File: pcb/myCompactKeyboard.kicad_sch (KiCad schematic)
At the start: 245 parts, among them J1 OLED_128x64, SW1 RotaryEncoder_Switch, SW2 RotaryEncoder_Switch, U1 Raspberry_Pi_Pico

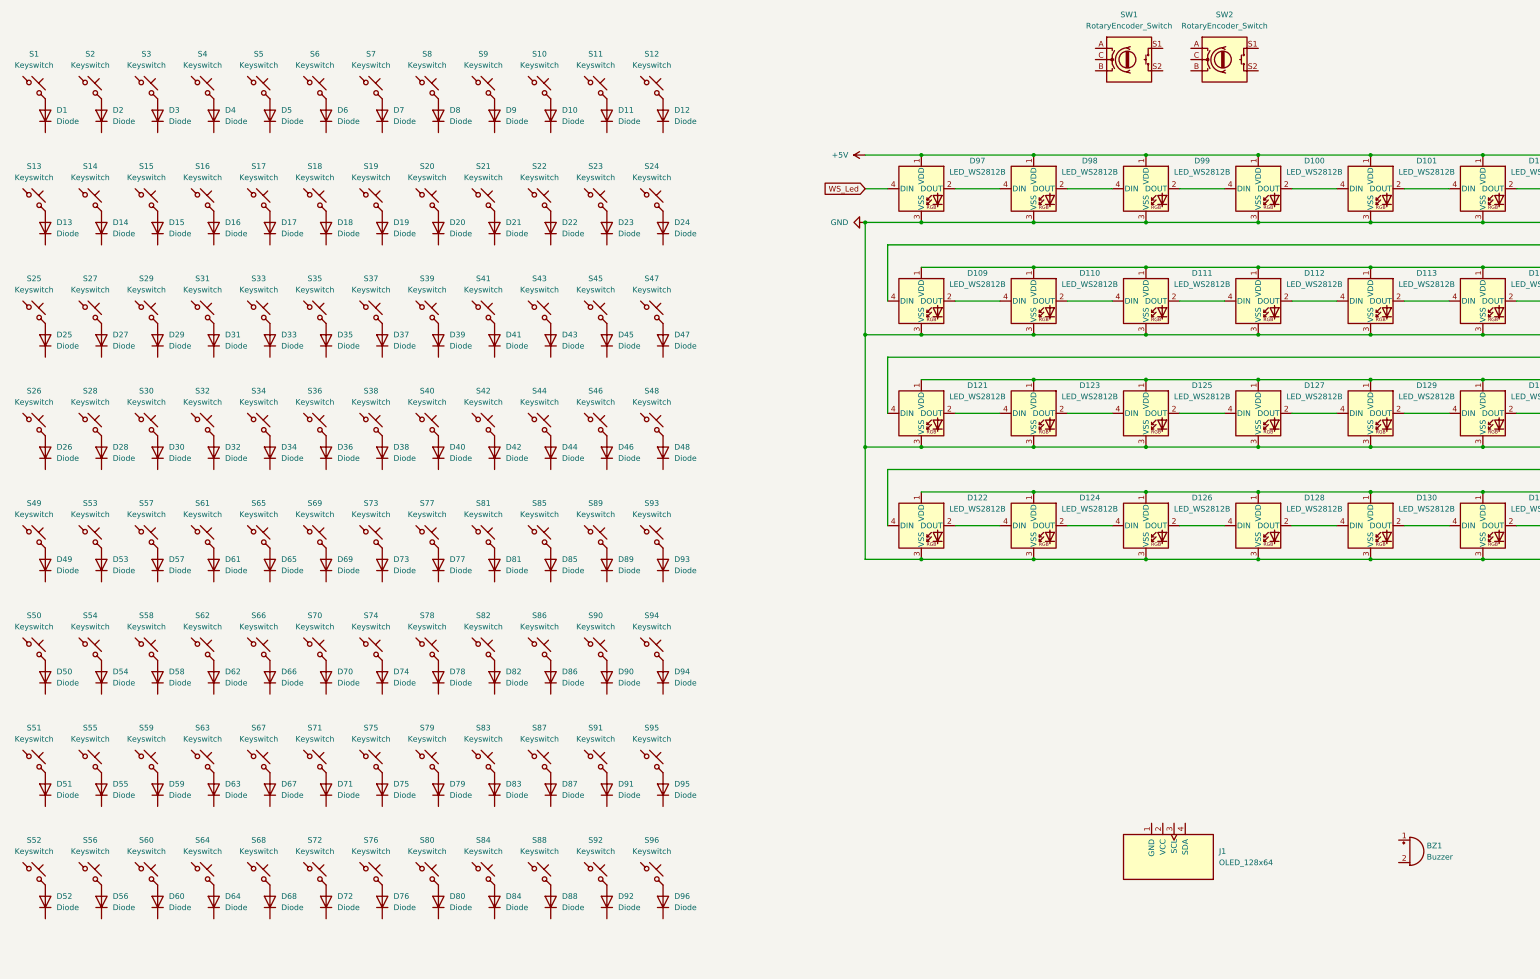
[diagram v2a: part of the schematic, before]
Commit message: wired the keys in the schematic
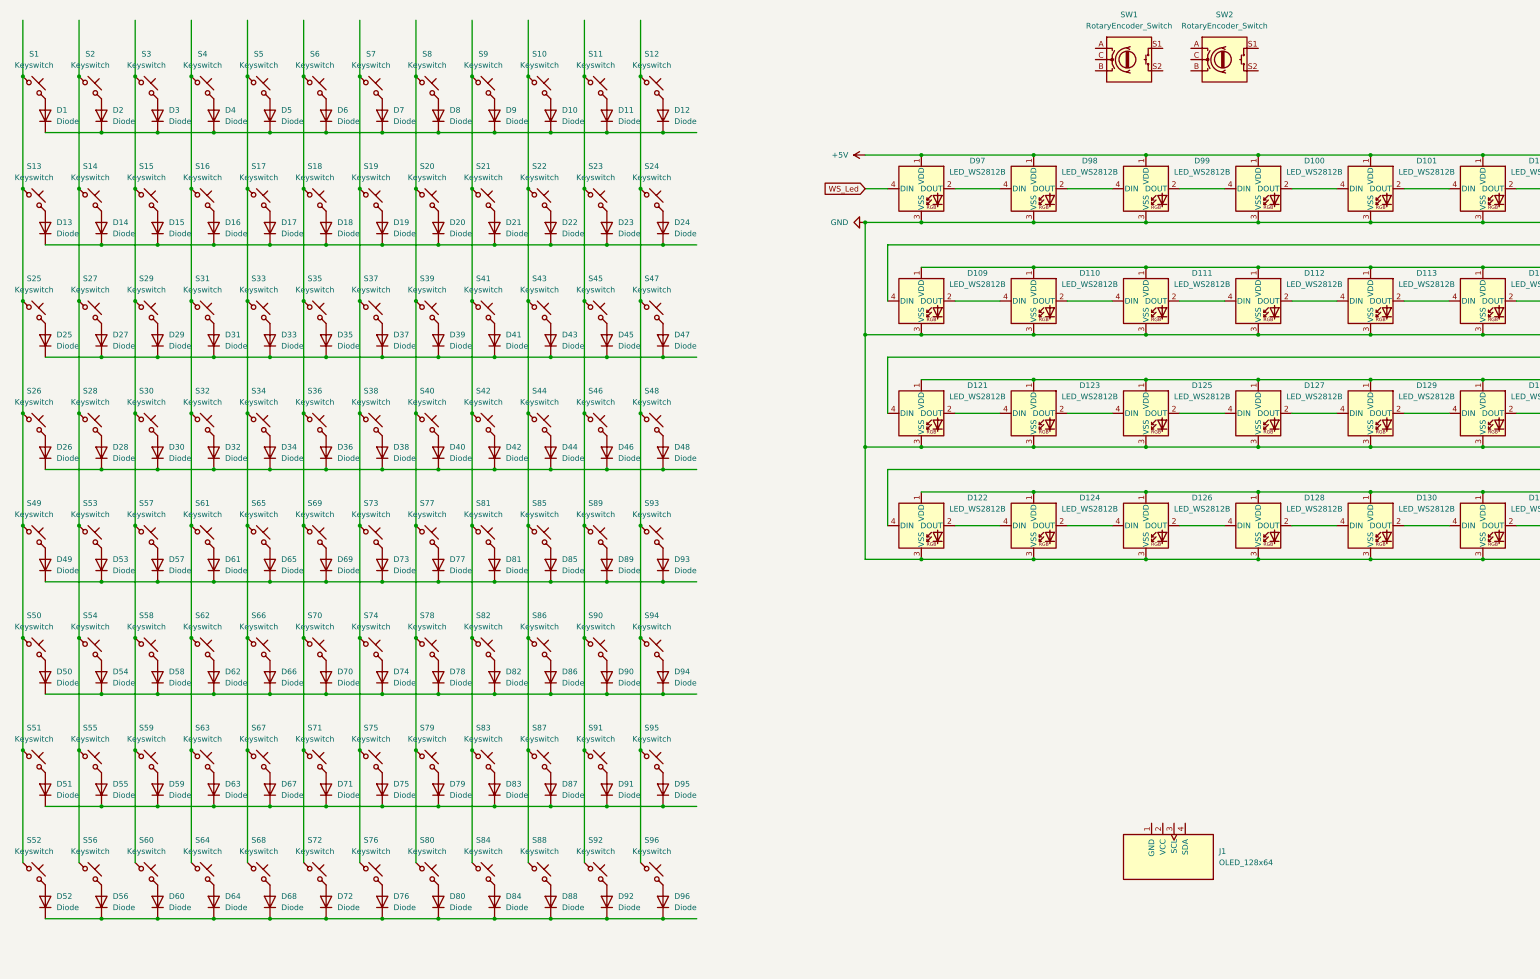
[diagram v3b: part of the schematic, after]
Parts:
- removed BZ1: Buzzer, symbol Device:Buzzer
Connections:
- net at S35.1: now also S18.1, S36.1, S6.1, S69.1, S70.1, S71.1, S72.1
- net at S58.1: now also S15.1, S29.1, S3.1, S30.1, S57.1, S59.1, S60.1
- net at S95.1: now also S12.1, S24.1, S47.1, S48.1, S93.1, S94.1, S96.1
- net at S13.1: now also S1.1, S25.1, S26.1, S49.1, S50.1, S51.1, S52.1
- net at S17.1: now also S33.1, S34.1, S5.1, S65.1, S66.1, S67.1, S68.1
- net at D8.1 (K): now also D1.1 (K), D10.1 (K), D11.1 (K), D12.1 (K), D2.1 (K), D3.1 (K), D4.1 (K), D5.1 (K), D6.1 (K), D7.1 (K), D9.1 (K)
- net at S19.1: now also S37.1, S38.1, S7.1, S73.1, S74.1, S75.1, S76.1
- net at D76.1 (K): now also D52.1 (K), D56.1 (K), D60.1 (K), D64.1 (K), D68.1 (K), D72.1 (K), D80.1 (K), D84.1 (K), D88.1 (K), D92.1 (K), D96.1 (K)
- net at D57.1 (K): now also D49.1 (K), D53.1 (K), D61.1 (K), D65.1 (K), D69.1 (K), D73.1 (K), D77.1 (K), D81.1 (K), D85.1 (K), D89.1 (K), D93.1 (K)
- net at S23.1: now also S11.1, S45.1, S46.1, S89.1, S90.1, S91.1, S92.1
- net at D59.1 (K): now also D51.1 (K), D55.1 (K), D63.1 (K), D67.1 (K), D71.1 (K), D75.1 (K), D79.1 (K), D83.1 (K), D87.1 (K), D91.1 (K), D95.1 (K)
- net at D54.1 (K): now also D50.1 (K), D58.1 (K), D62.1 (K), D66.1 (K), D70.1 (K), D74.1 (K), D78.1 (K), D82.1 (K), D86.1 (K), D90.1 (K), D94.1 (K)
- net at S78.1: now also S20.1, S39.1, S40.1, S77.1, S79.1, S8.1, S80.1
- net at D15.1 (K): now also D13.1 (K), D14.1 (K), D16.1 (K), D17.1 (K), D18.1 (K), D19.1 (K), D20.1 (K), D21.1 (K), D22.1 (K), D23.1 (K), D24.1 (K)
- net at D28.1 (K): now also D26.1 (K), D30.1 (K), D32.1 (K), D34.1 (K), D36.1 (K), D38.1 (K), D40.1 (K), D42.1 (K), D44.1 (K), D46.1 (K), D48.1 (K)
- net at S14.1: now also S2.1, S27.1, S28.1, S53.1, S54.1, S55.1, S56.1
- net at D25.1 (K): now also D27.1 (K), D29.1 (K), D31.1 (K), D33.1 (K), D35.1 (K), D37.1 (K), D39.1 (K), D41.1 (K), D43.1 (K), D45.1 (K), D47.1 (K)
- net at S84.1: now also S21.1, S41.1, S42.1, S81.1, S82.1, S83.1, S9.1
- net at S10.1: now also S22.1, S43.1, S44.1, S85.1, S86.1, S87.1, S88.1
- net at S63.1: now also S16.1, S31.1, S32.1, S4.1, S61.1, S62.1, S64.1

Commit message: converted the light matrix to a full 12x8
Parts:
- added D145, D146, D147, D148, D149, D150, D151, D152, D153, D154, D155, D156, D157, D158, D159, D160, D161, D162, D163, D164, D165, D166, D167, D168, D169, D170, D171, D172, D173, D174, D175, D176, D177, D178, D179, D180, D181, D182, D183, D184, D185, D186, D187, D188, D189, D190, D191, D192: LED_WS2812B, ScottoKeebs_Components:LED_WS2812B, symbol ScottoKeebs:LED_WS2812B
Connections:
- net +5V: now also D145.1 (VDD), D146.1 (VDD), D147.1 (VDD), D148.1 (VDD), D149.1 (VDD), D150.1 (VDD), D151.1 (VDD), D152.1 (VDD), D153.1 (VDD), D154.1 (VDD), D155.1 (VDD), D156.1 (VDD), D157.1 (VDD), D158.1 (VDD), D159.1 (VDD), D160.1 (VDD), D161.1 (VDD), D162.1 (VDD), D163.1 (VDD), D164.1 (VDD), D165.1 (VDD), D166.1 (VDD), D167.1 (VDD), D168.1 (VDD), D169.1 (VDD), D170.1 (VDD), D171.1 (VDD), D172.1 (VDD), D173.1 (VDD), D174.1 (VDD), D175.1 (VDD), D176.1 (VDD), D177.1 (VDD), D178.1 (VDD), D179.1 (VDD), D180.1 (VDD), D181.1 (VDD), D182.1 (VDD), D183.1 (VDD), D184.1 (VDD), D185.1 (VDD), D186.1 (VDD), D187.1 (VDD), D188.1 (VDD), D189.1 (VDD), D190.1 (VDD), D191.1 (VDD), D192.1 (VDD); no longer D100.3 (VSS), D101.3 (VSS), D102.3 (VSS), D103.3 (VSS), D104.3 (VSS), D105.3 (VSS), D106.3 (VSS), D107.3 (VSS), D108.3 (VSS), D109.3 (VSS), D110.3 (VSS), D111.3 (VSS), D112.3 (VSS), D113.3 (VSS), D114.3 (VSS), D115.3 (VSS), D116.3 (VSS), D117.3 (VSS), D118.3 (VSS), D119.3 (VSS), D120.3 (VSS), D121.3 (VSS), D122.3 (VSS), D123.3 (VSS), D124.3 (VSS), D125.3 (VSS), D126.3 (VSS), D127.3 (VSS), D128.3 (VSS), D129.3 (VSS), D130.3 (VSS), D131.3 (VSS), D132.3 (VSS), D133.3 (VSS), D134.3 (VSS), D135.3 (VSS), D136.3 (VSS), D137.3 (VSS), D138.3 (VSS), D139.3 (VSS), D140.3 (VSS), D141.3 (VSS), D142.3 (VSS), D143.3 (VSS), D144.3 (VSS), D97.3 (VSS), D98.3 (VSS), D99.3 (VSS), U1.23 (GND)
- net at D144.2 (DOUT): now also D145.4 (DIN)
- new net: D155.2 (DOUT), D159.4 (DIN)
- new net: D151.2 (DOUT), D155.4 (DIN)
- new net: D183.2 (DOUT), D187.4 (DIN)
- new net: D179.2 (DOUT), D183.4 (DIN)
- new net: D178.2 (DOUT), D182.4 (DIN)
- new net: D174.2 (DOUT), D178.4 (DIN)
- new net: D177.2 (DOUT), D181.4 (DIN)
- new net: D173.2 (DOUT), D177.4 (DIN)
- new net: D187.2 (DOUT), D191.4 (DIN)
- new net: D175.2 (DOUT), D179.4 (DIN)
- new net: D147.2 (DOUT), D151.4 (DIN)
- new net: D147.4 (DIN), D190.2 (DOUT)
- new net: D163.2 (DOUT), D167.4 (DIN)
- new net: D159.2 (DOUT), D163.4 (DIN)
- new net: D162.2 (DOUT), D166.4 (DIN)
- new net: D158.2 (DOUT), D162.4 (DIN)
- new net: D188.2 (DOUT), D192.4 (DIN)
- new net: D184.2 (DOUT), D188.4 (DIN)
- new net: D170.2 (DOUT), D174.4 (DIN)
- new net: D166.2 (DOUT), D170.4 (DIN)
- new net: D176.2 (DOUT), D180.4 (DIN)
- new net: D172.2 (DOUT), D176.4 (DIN)
- new net: D152.2 (DOUT), D156.4 (DIN)
- new net: D148.2 (DOUT), D152.4 (DIN)
- new net: D169.2 (DOUT), D173.4 (DIN)
- new net: D165.2 (DOUT), D169.4 (DIN)
- new net: D181.2 (DOUT), D185.4 (DIN)
- new net: D168.2 (DOUT), D172.4 (DIN)
- new net: D180.2 (DOUT), D184.4 (DIN)
- new net: D171.2 (DOUT), D175.4 (DIN)
- new net: D185.2 (DOUT), D189.4 (DIN)
- new net: D167.2 (DOUT), D171.4 (DIN)
- new net: D157.2 (DOUT), D161.4 (DIN)
- new net: D153.2 (DOUT), D157.4 (DIN)
- new net: D145.2 (DOUT), D149.4 (DIN)
- new net: D182.2 (DOUT), D186.4 (DIN)
- new net: D149.2 (DOUT), D153.4 (DIN)
- new net: D154.2 (DOUT), D158.4 (DIN)
- new net: D164.2 (DOUT), D168.4 (DIN)
- new net: D160.2 (DOUT), D164.4 (DIN)
- new net: D148.4 (DIN), D191.2 (DOUT)
- new net: D186.2 (DOUT), D190.4 (DIN)
- new net: D150.2 (DOUT), D154.4 (DIN)
- new net: D146.4 (DIN), D189.2 (DOUT)
- new net: D156.2 (DOUT), D160.4 (DIN)
- new net: D146.2 (DOUT), D150.4 (DIN)
- new net: D161.2 (DOUT), D165.4 (DIN)
- new net GND: D100.3 (VSS), D101.3 (VSS), D102.3 (VSS), D103.3 (VSS), D104.3 (VSS), D105.3 (VSS), D106.3 (VSS), D107.3 (VSS), D108.3 (VSS), D109.3 (VSS), D110.3 (VSS), D111.3 (VSS), D112.3 (VSS), D113.3 (VSS), D114.3 (VSS), D115.3 (VSS), D116.3 (VSS), D117.3 (VSS), D118.3 (VSS), D119.3 (VSS), D120.3 (VSS), D121.3 (VSS), D122.3 (VSS), D123.3 (VSS), D124.3 (VSS), D125.3 (VSS), D126.3 (VSS), D127.3 (VSS), D128.3 (VSS), D129.3 (VSS), D130.3 (VSS), D131.3 (VSS), D132.3 (VSS), D133.3 (VSS), D134.3 (VSS), D135.3 (VSS), D136.3 (VSS), D137.3 (VSS), D138.3 (VSS), D139.3 (VSS), D140.3 (VSS), D141.3 (VSS), D142.3 (VSS), D143.3 (VSS), D144.3 (VSS), D145.3 (VSS), D146.3 (VSS), D147.3 (VSS), D148.3 (VSS), D149.3 (VSS), D150.3 (VSS), D151.3 (VSS), D152.3 (VSS), D153.3 (VSS), D154.3 (VSS), D155.3 (VSS), D156.3 (VSS), D157.3 (VSS), D158.3 (VSS), D159.3 (VSS), D160.3 (VSS), D161.3 (VSS), D162.3 (VSS), D163.3 (VSS), D164.3 (VSS), D165.3 (VSS), D166.3 (VSS), D167.3 (VSS), D168.3 (VSS), D169.3 (VSS), D170.3 (VSS), D171.3 (VSS), D172.3 (VSS), D173.3 (VSS), D174.3 (VSS), D175.3 (VSS), D176.3 (VSS), D177.3 (VSS), D178.3 (VSS), D179.3 (VSS), D180.3 (VSS), D181.3 (VSS), D182.3 (VSS), D183.3 (VSS), D184.3 (VSS), D185.3 (VSS), D186.3 (VSS), D187.3 (VSS), D188.3 (VSS), D189.3 (VSS), D190.3 (VSS), D191.3 (VSS), D192.3 (VSS), D97.3 (VSS), D98.3 (VSS), D99.3 (VSS), U1.23 (GND)
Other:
- moved on the sheet: J1, U1

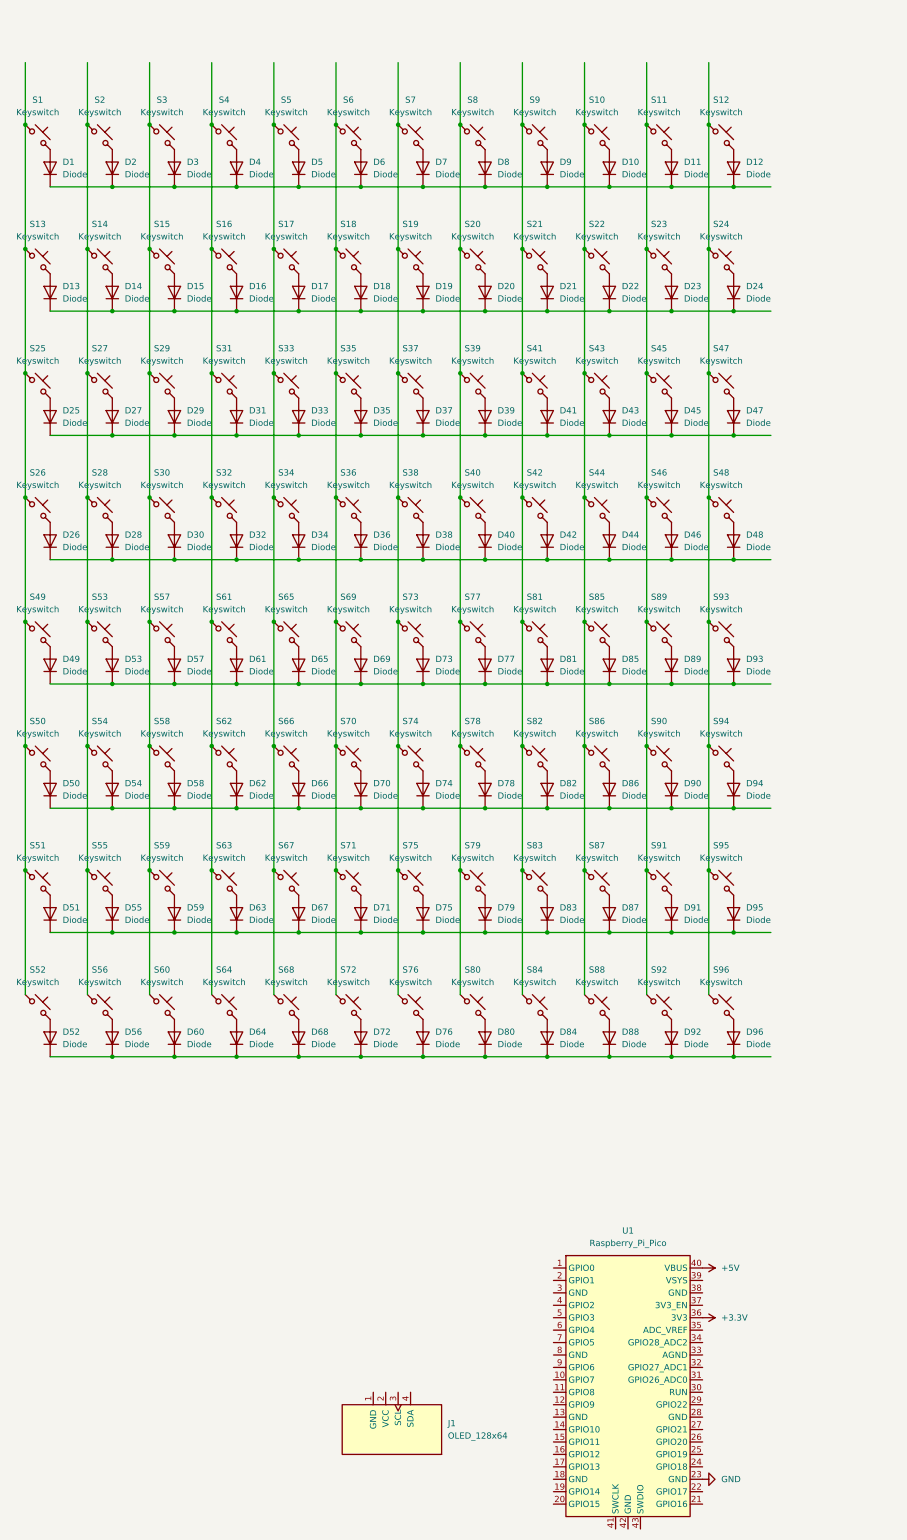
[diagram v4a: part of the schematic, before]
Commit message: added labels to switch matrix
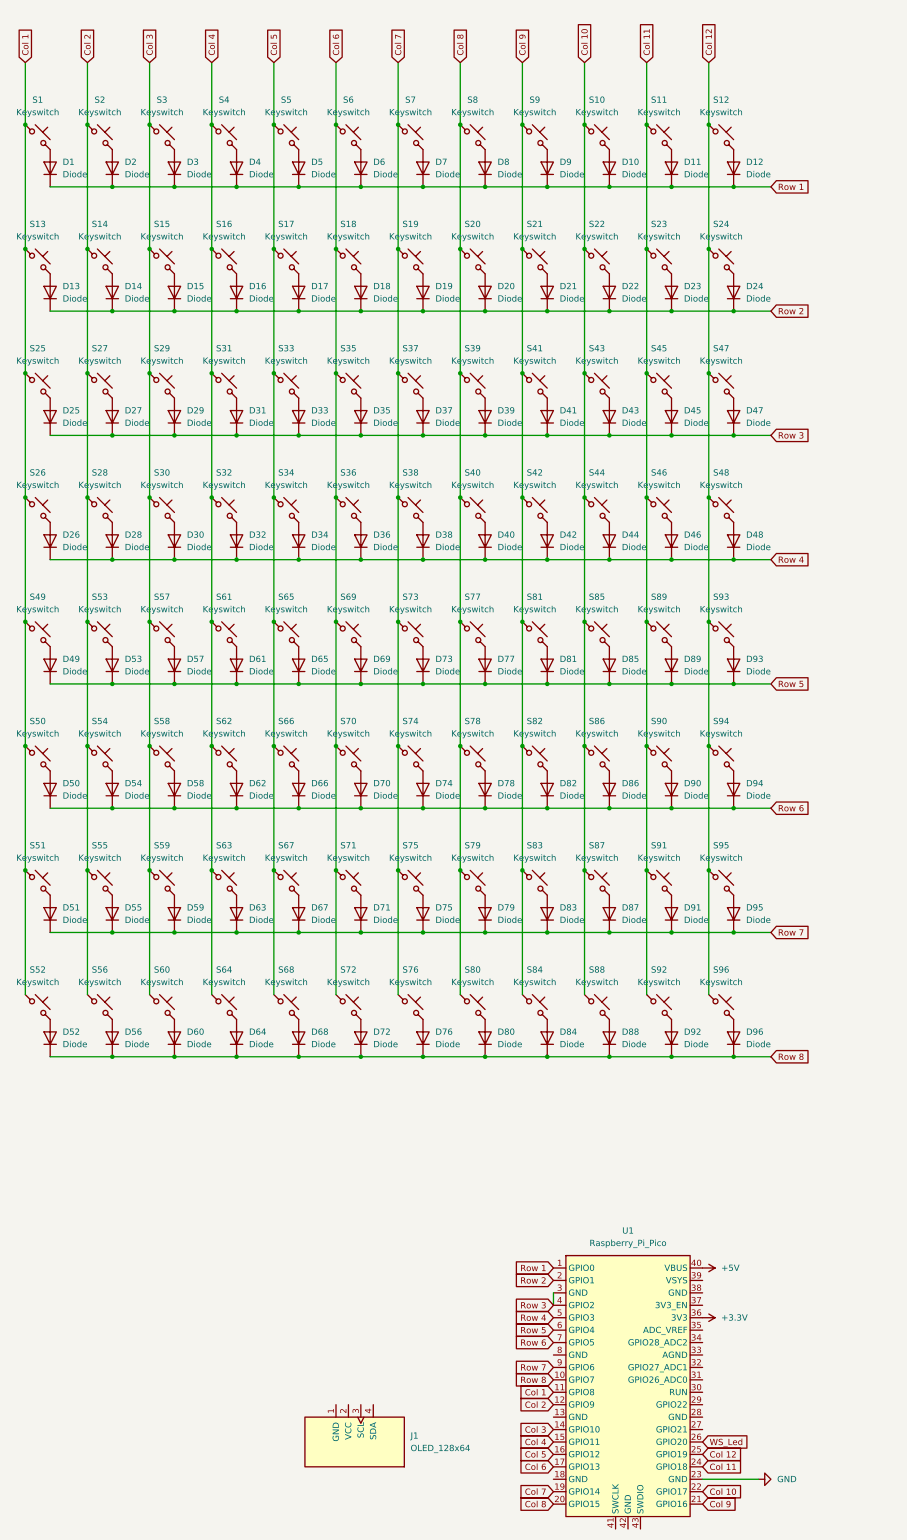
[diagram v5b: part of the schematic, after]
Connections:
- net WS_Led: now also U1.26 (GPIO20)
- net Col 6: now reaches S18.1, S35.1, S36.1, S6.1, S69.1, S70.1, S71.1, S72.1
- net Col 6: now also U1.17 (GPIO13)
- net Col 3: now reaches S15.1, S29.1, S3.1, S30.1, S57.1, S58.1, S59.1, S60.1
- net Col 3: now also U1.14 (GPIO10)
- net Col 12: now reaches S12.1, S24.1, S47.1, S48.1, S93.1, S94.1, S95.1, S96.1
- net Col 12: now also U1.25 (GPIO19)
- net Col 1: now reaches S1.1, S13.1, S25.1, S26.1, S49.1, S50.1, S51.1, S52.1
- net Col 1: now also U1.11 (GPIO8)
- net Col 5: now reaches S17.1, S33.1, S34.1, S5.1, S65.1, S66.1, S67.1, S68.1
- net Col 5: now also U1.16 (GPIO12)
- net Row 1: now reaches D1.1 (K), D10.1 (K), D11.1 (K), D12.1 (K), D2.1 (K), D3.1 (K), D4.1 (K), D5.1 (K), D6.1 (K), D7.1 (K), D8.1 (K), D9.1 (K)
- net Row 1: now also U1.1 (GPIO0)
- net Col 7: now reaches S19.1, S37.1, S38.1, S7.1, S73.1, S74.1, S75.1, S76.1
- net Col 7: now also U1.19 (GPIO14)
- net Row 8: now reaches D52.1 (K), D56.1 (K), D60.1 (K), D64.1 (K), D68.1 (K), D72.1 (K), D76.1 (K), D80.1 (K), D84.1 (K), D88.1 (K), D92.1 (K), D96.1 (K)
- net Row 8: now also U1.10 (GPIO7)
- net Row 5: now reaches D49.1 (K), D53.1 (K), D57.1 (K), D61.1 (K), D65.1 (K), D69.1 (K), D73.1 (K), D77.1 (K), D81.1 (K), D85.1 (K), D89.1 (K), D93.1 (K)
- net Row 5: now also U1.6 (GPIO4)
- net Col 11: now reaches S11.1, S23.1, S45.1, S46.1, S89.1, S90.1, S91.1, S92.1
- net Col 11: now also U1.24 (GPIO18)
- net Row 7: now reaches D51.1 (K), D55.1 (K), D59.1 (K), D63.1 (K), D67.1 (K), D71.1 (K), D75.1 (K), D79.1 (K), D83.1 (K), D87.1 (K), D91.1 (K), D95.1 (K)
- net Row 7: now also U1.9 (GPIO6)
- net Row 6: now reaches D50.1 (K), D54.1 (K), D58.1 (K), D62.1 (K), D66.1 (K), D70.1 (K), D74.1 (K), D78.1 (K), D82.1 (K), D86.1 (K), D90.1 (K), D94.1 (K)
- net Row 6: now also U1.7 (GPIO5)
- net Col 8: now reaches S20.1, S39.1, S40.1, S77.1, S78.1, S79.1, S8.1, S80.1
- net Col 8: now also U1.20 (GPIO15)
- net Row 2: now reaches D13.1 (K), D14.1 (K), D15.1 (K), D16.1 (K), D17.1 (K), D18.1 (K), D19.1 (K), D20.1 (K), D21.1 (K), D22.1 (K), D23.1 (K), D24.1 (K)
- net Row 2: now also U1.2 (GPIO1)
- net Row 4: now reaches D26.1 (K), D28.1 (K), D30.1 (K), D32.1 (K), D34.1 (K), D36.1 (K), D38.1 (K), D40.1 (K), D42.1 (K), D44.1 (K), D46.1 (K), D48.1 (K)
- net Row 4: now also U1.5 (GPIO3)
- net Col 2: now reaches S14.1, S2.1, S27.1, S28.1, S53.1, S54.1, S55.1, S56.1
- net Col 2: now also U1.12 (GPIO9)
- net Row 3: now reaches D25.1 (K), D27.1 (K), D29.1 (K), D31.1 (K), D33.1 (K), D35.1 (K), D37.1 (K), D39.1 (K), D41.1 (K), D43.1 (K), D45.1 (K), D47.1 (K)
- net Row 3: now also U1.3 (GND), U1.4 (GPIO2)
- net Col 9: now reaches S21.1, S41.1, S42.1, S81.1, S82.1, S83.1, S84.1, S9.1
- net Col 9: now also U1.21 (GPIO16)
- net Col 10: now reaches S10.1, S22.1, S43.1, S44.1, S85.1, S86.1, S87.1, S88.1
- net Col 10: now also U1.22 (GPIO17)
- net Col 4: now reaches S16.1, S31.1, S32.1, S4.1, S61.1, S62.1, S63.1, S64.1
- net Col 4: now also U1.15 (GPIO11)
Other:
- moved on the sheet: J1
